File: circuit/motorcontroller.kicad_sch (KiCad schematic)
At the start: 12 parts, among them J1 RJ45, M1 Motor_Servo, M2 Motor_Servo, SW1 SW_SPDT

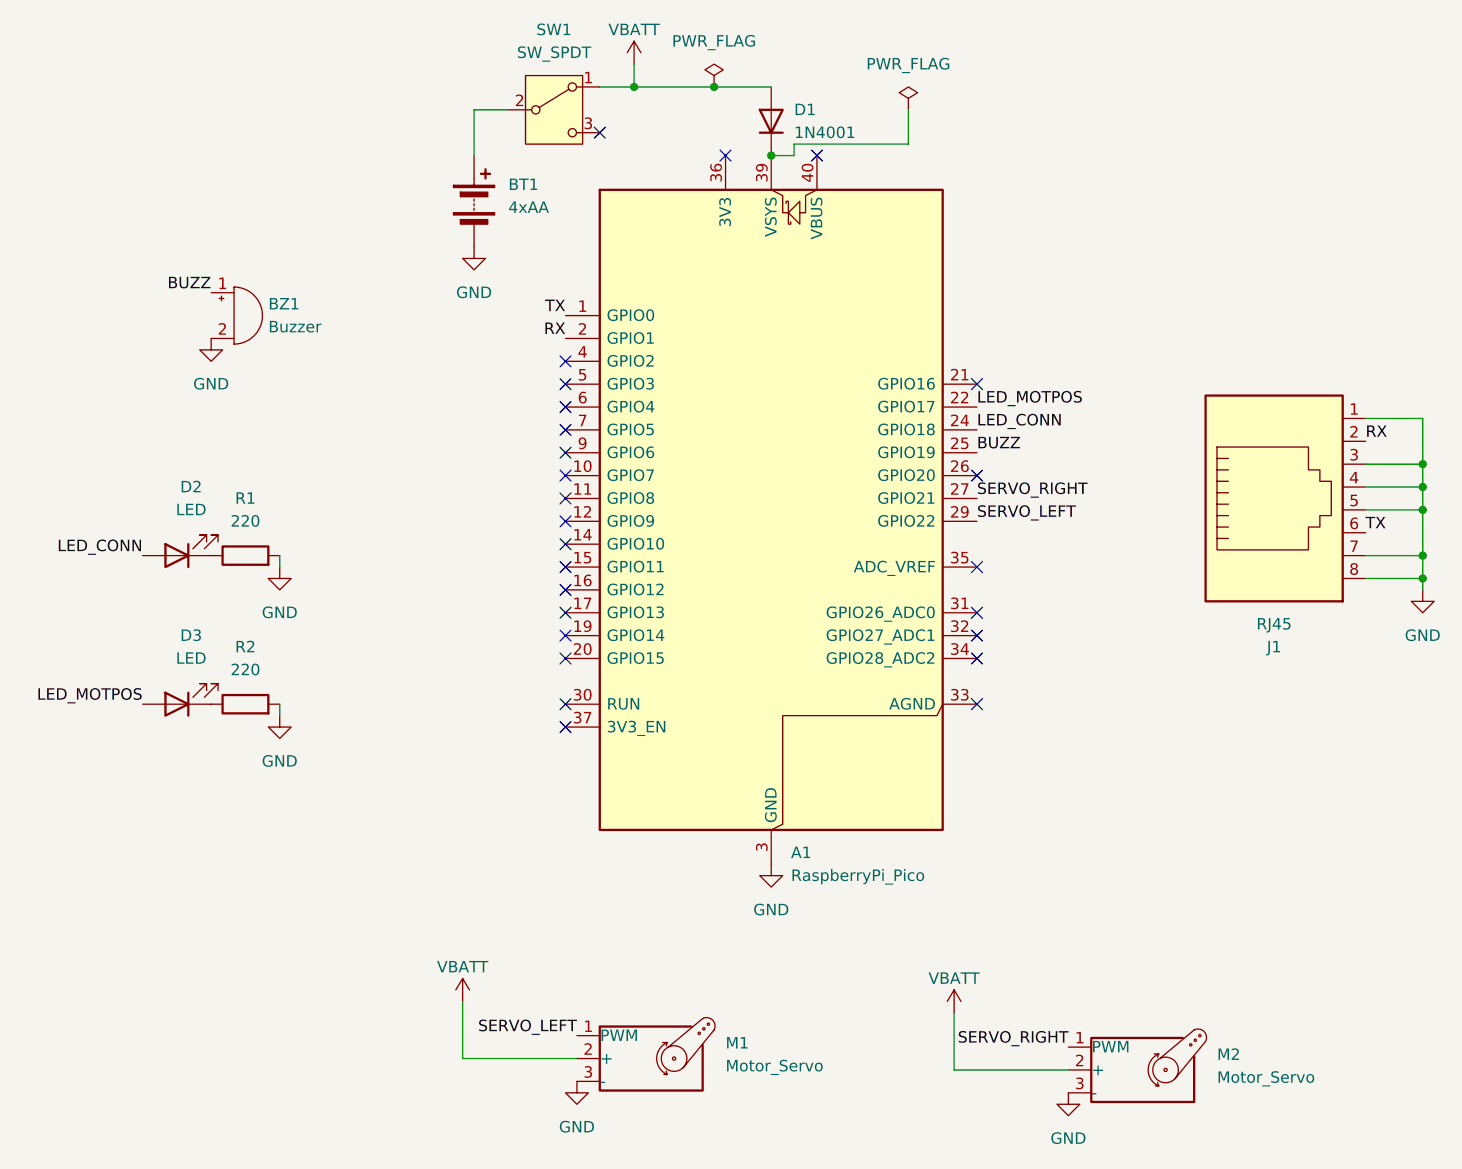
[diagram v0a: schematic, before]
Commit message: add motor controller wiring diagram
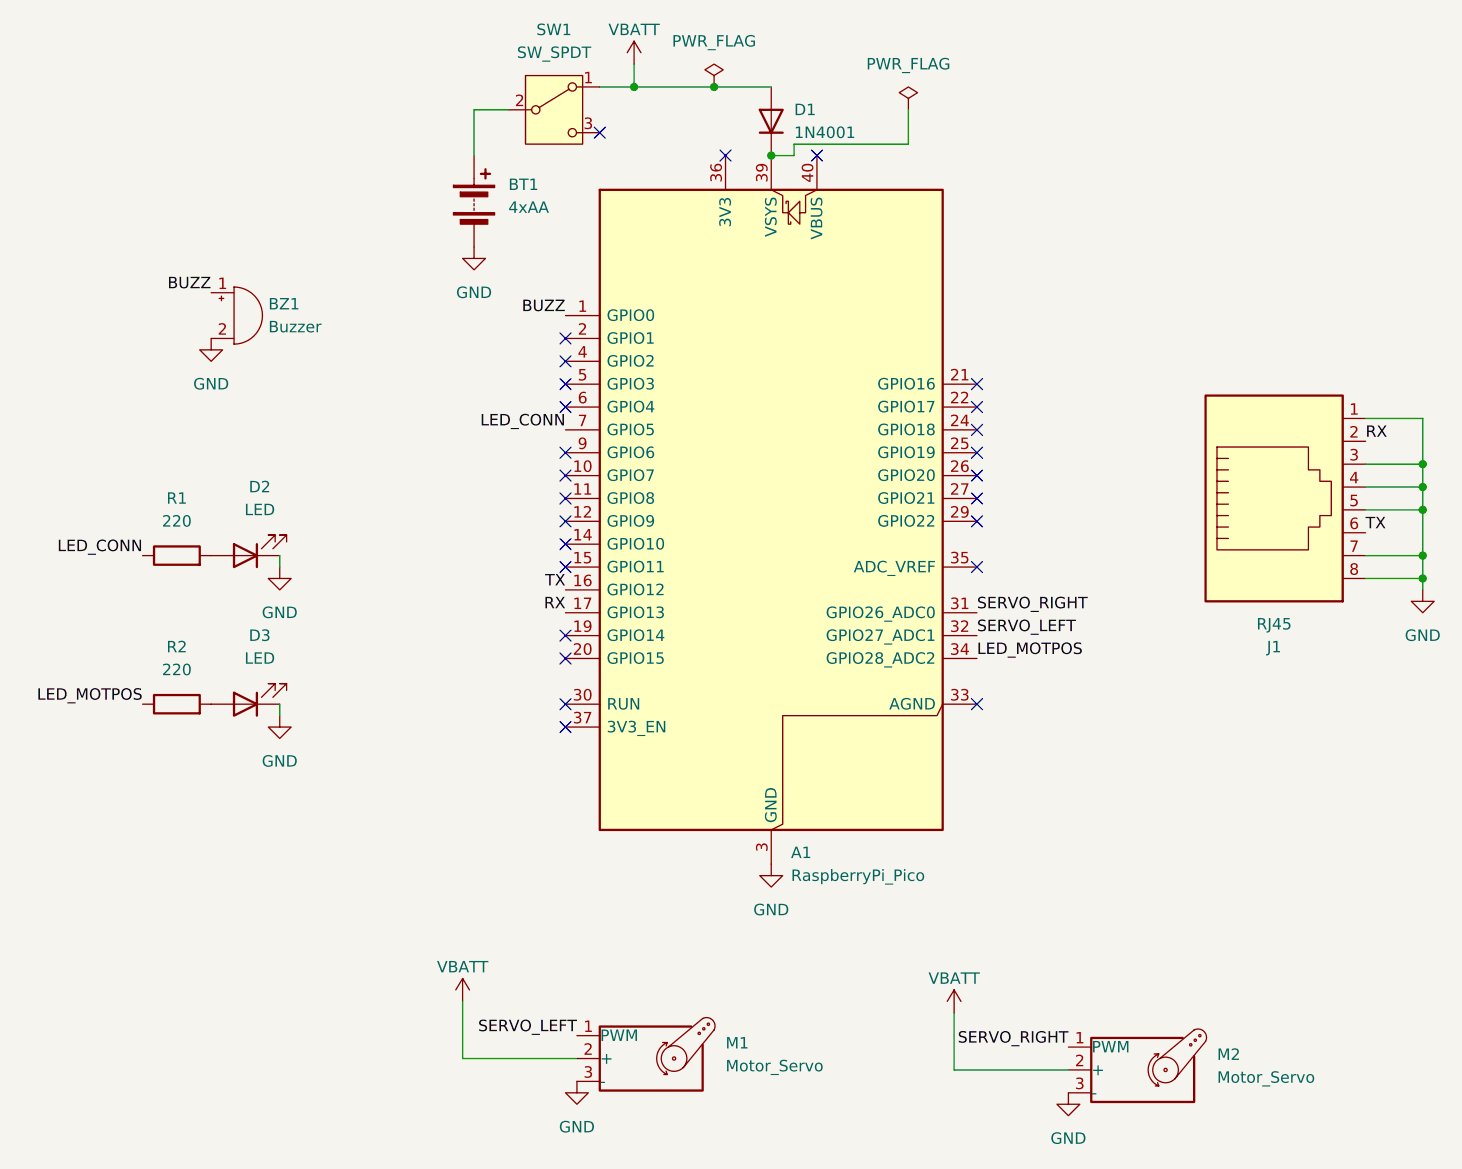
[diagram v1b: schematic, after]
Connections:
- net BUZZ: now also A1.1 (GPIO0); no longer A1.25 (GPIO19)
- net GND: now also D2.1 (K), D3.1 (K); no longer R1.2, R2.2
- net LED_CONN: now also A1.7 (GPIO5), R1.1; no longer A1.24 (GPIO18), D2.2 (A)
- net LED_MOTPOS: now also A1.34 (GPIO28_ADC2), R2.1; no longer A1.22 (GPIO17), D3.2 (A)
- net RX: now also A1.17 (GPIO13); no longer A1.2 (GPIO1)
- net SERVO_LEFT: now also A1.32 (GPIO27_ADC1); no longer A1.29 (GPIO22)
- net SERVO_RIGHT: now also A1.31 (GPIO26_ADC0); no longer A1.27 (GPIO21)
- net TX: now also A1.16 (GPIO12); no longer A1.1 (GPIO0)
- new net: D2.2 (A), R1.2
- new net: D3.2 (A), R2.2
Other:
- moved on the sheet: D2, D3, R1, R2
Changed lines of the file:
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@@
 	)
 	(no_connect
-		(at 96.52 80.01)
+		(at 142.24 72.39)
 	)
 	(no_connect
@@
 	)
 	(no_connect
+		(at 96.52 52.07)
+	)
+	(no_connect
 		(at 96.52 67.31)
 	)
@@
 	)
 	(no_connect
-		(at 142.24 87.63)
-	)
-	(no_connect
-		(at 142.24 85.09)
-	)
-	(no_connect
 		(at 96.52 59.69)
 	)
@@
 	)
 	(no_connect
+		(at 142.24 64.77)
+	)
+	(no_connect
+		(at 142.24 62.23)
+	)
+	(no_connect
 		(at 96.52 77.47)
 	)
@@
 	)
 	(no_connect
-		(at 96.52 62.23)
-	)
-	(no_connect
 		(at 142.24 92.71)
 	)
@@
 	)
 	(no_connect
+		(at 142.24 69.85)
+	)
+	(no_connect
 		(at 96.52 69.85)
 	)
 	(no_connect
-		(at 96.52 82.55)
-	)
-	(no_connect
-		(at 142.24 82.55)
+		(at 142.24 59.69)
 	)
 	(no_connect
@@
 	)
 	(label "SERVO_RIGHT"
-		(at 142.24 69.85 0)
+		(at 142.24 82.55 0)
 		(effects
 			(font
@@
 	)
 	(label "LED_CONN"
-		(at 142.24 62.23 0)
+		(at 96.52 62.23 180)
 		(effects
 			(font
 				(size 1.27 1.27)
 			)
-			(justify left bottom)
+			(justify right bottom)
 		)
 	)
 	(label "RX"
-		(at 96.52 52.07 180)
+		(at 96.52 82.55 180)
 		(effects
 			(font
@@
 	)
 	(label "LED_MOTPOS"
-		(at 142.24 59.69 0)
+		(at 142.24 87.63 0)
 		(effects
 			(font
@@
 	)
 	(label "TX"
+		(at 96.52 80.01 180)
+		(effects
+			(font
+				(size 1.27 1.27)
+			)
+			(justify right bottom)
+		)
+	)
+	(label "SERVO_LEFT"
+		(at 142.24 85.09 0)
+		(effects
+			(font
+				(size 1.27 1.27)
+			)
+			(justify left bottom)
+		)
+	)
+	(label "BUZZ"
 		(at 96.52 49.53 180)
 		(effects
@@
 			)
 			(justify right bottom)
-		)
-	)
-	(label "SERVO_LEFT"
-		(at 142.24 72.39 0)
-		(effects
-			(font
-				(size 1.27 1.27)
-			)
-			(justify left bottom)
-		)
-	)
-	(label "BUZZ"
-		(at 142.24 64.77 0)
-		(effects
-			(font
-				(size 1.27 1.27)
-			)
-			(justify left bottom)
 		)
 	)
@@
 	(symbol
 		(lib_id "Device:R")
-		(at 60.96 76.2 90)
+		(at 53.34 76.2 90)
 		(unit 1)
 		(exclude_from_sim no)
@@
 		(fields_autoplaced yes)
 		(property "Reference" "R1"
-			(at 60.96 69.85 90)
+			(at 53.34 69.85 90)
 			(effects
 				(font
@@
 		)
 		(property "Value" "220"
-			(at 60.96 72.39 90)
+			(at 53.34 72.39 90)
 			(effects
 				(font
@@
 		)
 		(property "Footprint" ""
-			(at 60.96 77.978 90)
+			(at 53.34 77.978 90)
 			(effects
 				(font
@@
 		)
 		(property "Datasheet" "~"
-			(at 60.96 76.2 0)
+			(at 53.34 76.2 0)
 			(effects
 				(font
@@
 		)
 		(property "Description" "Resistor"
-			(at 60.96 76.2 0)
+			(at 53.34 76.2 0)
 			(effects
 				(font
@@
 	(symbol
 		(lib_id "Device:LED")
-		(at 53.34 92.71 180)
+		(at 60.96 92.71 180)
 		(unit 1)
 		(exclude_from_sim no)
@@
 		(fields_autoplaced yes)
 		(property "Reference" "D3"
-			(at 54.9275 85.09 0)
+			(at 62.5475 85.09 0)
 			(effects
 				(font
@@
 		)
 		(property "Value" "LED"
-			(at 54.9275 87.63 0)
+			(at 62.5475 87.63 0)
 			(effects
 				(font
@@
 		)
 		(property "Footprint" ""
-			(at 53.34 92.71 0)
+			(at 60.96 92.71 0)
 			(effects
 				(font
@@
 		)
 		(property "Datasheet" "~"
-			(at 53.34 92.71 0)
+			(at 60.96 92.71 0)
 			(effects
 				(font
@@
 		)
 		(property "Description" "Light emitting diode"
-			(at 53.34 92.71 0)
+			(at 60.96 92.71 0)
 			(effects
 				(font
@@
 	(symbol
 		(lib_id "Device:R")
-		(at 60.96 92.71 90)
+		(at 53.34 92.71 90)
 		(unit 1)
 		(exclude_from_sim no)
@@
 		(fields_autoplaced yes)
 		(property "Reference" "R2"
-			(at 60.96 86.36 90)
+			(at 53.34 86.36 90)
 			(effects
 				(font
@@
 		)
 		(property "Value" "220"
-			(at 60.96 88.9 90)
+			(at 53.34 88.9 90)
 			(effects
 				(font
@@
 		)
 		(property "Footprint" ""
-			(at 60.96 94.488 90)
+			(at 53.34 94.488 90)
 			(effects
 				(font
@@
 		)
 		(property "Datasheet" "~"
-			(at 60.96 92.71 0)
+			(at 53.34 92.71 0)
 			(effects
 				(font
@@
 		)
 		(property "Description" "Resistor"
-			(at 60.96 92.71 0)
+			(at 53.34 92.71 0)
 			(effects
 				(font
@@
 	(symbol
 		(lib_id "Device:LED")
-		(at 53.34 76.2 180)
+		(at 60.96 76.2 180)
 		(unit 1)
 		(exclude_from_sim no)
@@
 		(fields_autoplaced yes)
 		(property "Reference" "D2"
-			(at 54.9275 68.58 0)
+			(at 62.5475 68.58 0)
 			(effects
 				(font
@@
 		)
 		(property "Value" "LED"
-			(at 54.9275 71.12 0)
+			(at 62.5475 71.12 0)
 			(effects
 				(font
@@
 		)
 		(property "Footprint" ""
-			(at 53.34 76.2 0)
+			(at 60.96 76.2 0)
 			(effects
 				(font
@@
 		)
 		(property "Datasheet" "~"
-			(at 53.34 76.2 0)
+			(at 60.96 76.2 0)
 			(effects
 				(font
@@
 		)
 		(property "Description" "Light emitting diode"
-			(at 53.34 76.2 0)
-			(effects
-				(font
+			(at 60.96 76.2 0)
+			(effects
+				(font

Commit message: update schematic to match wiring diagram
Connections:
- net LED_CONN: now also A1.24 (GPIO18); no longer A1.7 (GPIO5)
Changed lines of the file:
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@@
-	)
-	(no_connect
-		(at 142.24 62.23)
 	)
 	(no_connect
@@
 	(no_connect
 		(at 142.24 92.71)
+	)
+	(no_connect
+		(at 96.52 62.23)
 	)
 	(no_connect
@@
 	)
 	(label "LED_CONN"
-		(at 96.52 62.23 180)
+		(at 142.24 62.23 0)
 		(effects
 			(font
 				(size 1.27 1.27)
 			)
-			(justify right bottom)
-		)
-	)
+			(justify left bottom)
+		)
+	)

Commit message: fix short on motor controller board - oops
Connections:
- net GND: no longer J1.5
- no-connect marks 26 -> 27
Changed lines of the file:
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@@
-	)
-	(junction
-		(at 191.77 71.12)
-		(diameter 0)
-		(color 0 0 0 0)
 	)
 	(junction
@@
 	)
 	(no_connect
+		(at 185.42 71.12)
+	)
+	(no_connect
 		(at 100.33 29.21)
 	)
@@
 	(wire
 		(pts
-			(xy 191.77 71.12) (xy 191.77 68.58)
+			(xy 191.77 68.58) (xy 191.77 76.2)
 		)
 		(stroke
@@
 	(wire
 		(pts
-			(xy 185.42 71.12) (xy 191.77 71.12)
-		)
-		(stroke
-			(width 0)
-			(type default)
-		)
-	)
-	(wire
-		(pts
 			(xy 185.42 68.58) (xy 191.77 68.58)
 		)
@@
 		)
 		(stroke
-			(width 0)
-			(type default)
-		)
-	)
-	(wire
-		(pts
-			(xy 191.77 76.2) (xy 191.77 71.12)
-		)
-		(stroke
